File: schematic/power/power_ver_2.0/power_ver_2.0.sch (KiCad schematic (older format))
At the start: 47 parts, among them J1 PWM INPUT, J2 Audio OUTPUT, J3 Amp_Power, J4 Driver_power, Q1 IRF530A, Q2 IRF530A, Q3 IRF530A, Q4 IRF530A, U1 HIP4082IP

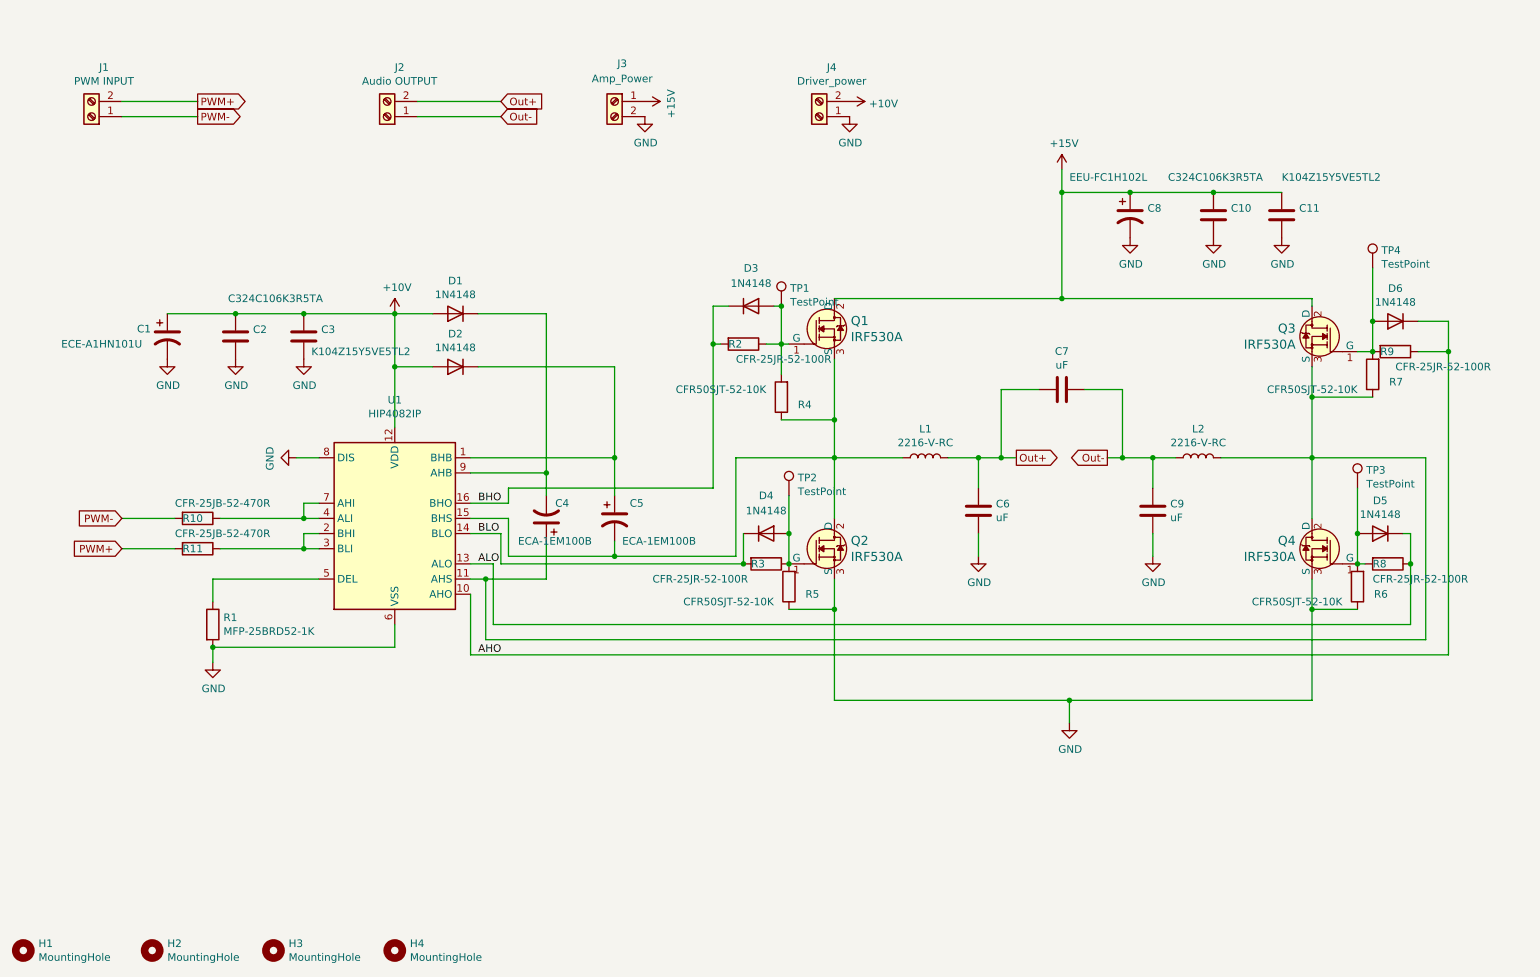
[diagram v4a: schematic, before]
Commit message: joint pcb power section
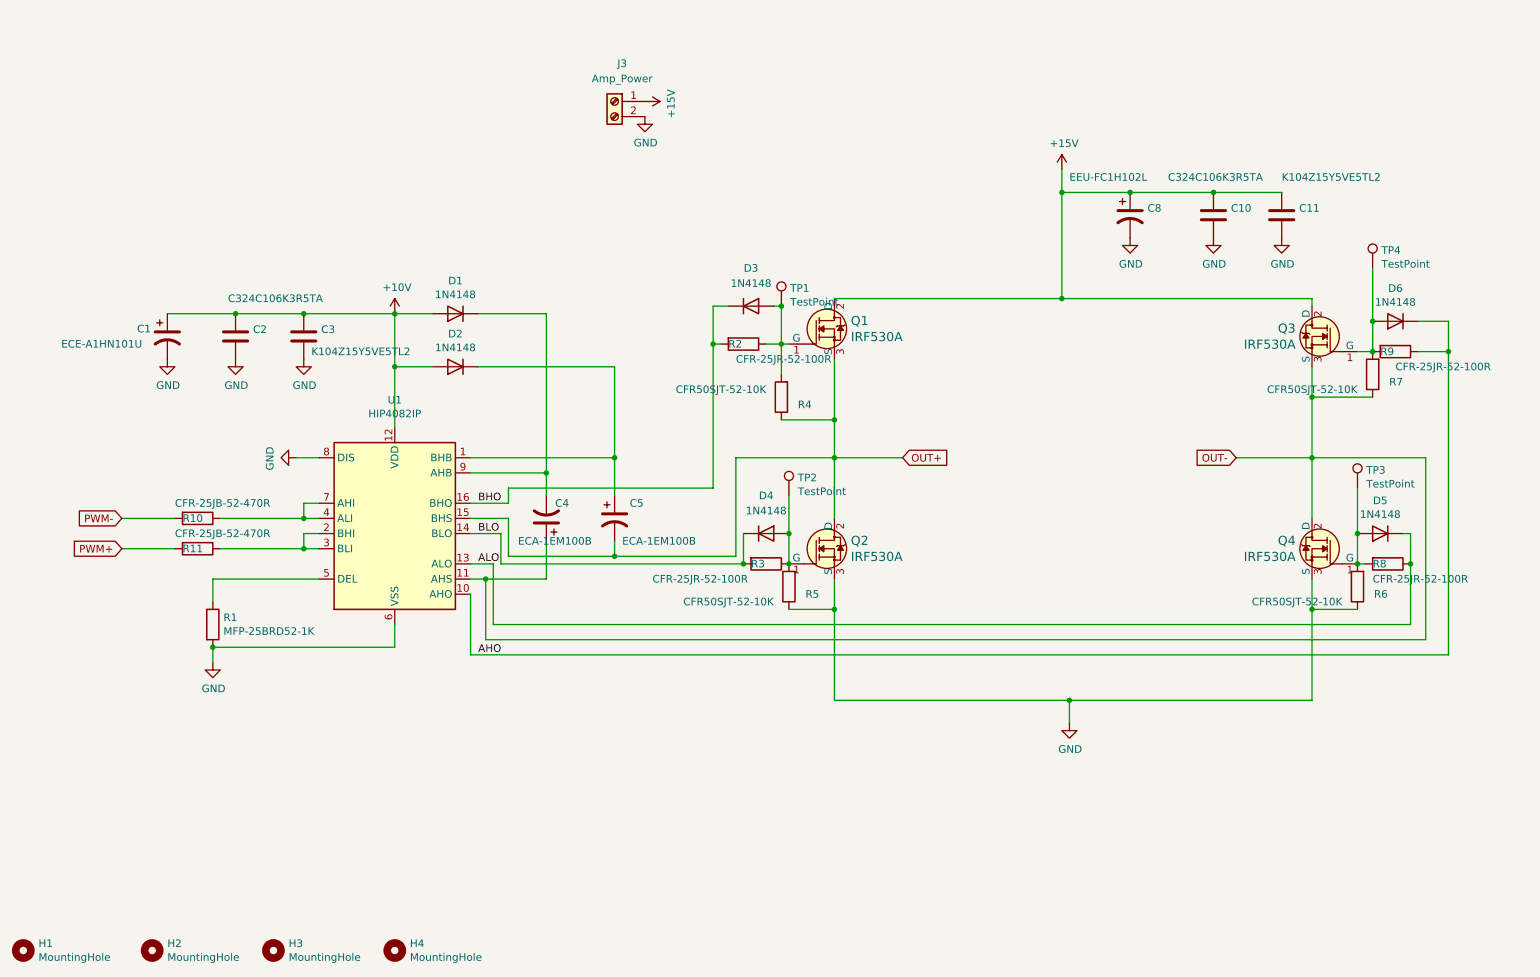
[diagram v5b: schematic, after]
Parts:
- removed C6, C7, C9: uF, Capacitor_THT:C_Radial_D10.0mm_H12.5mm_P5.00mm, symbol Device:C
- removed J1: PWM INPUT, TerminalBlock:TerminalBlock_Altech_AK300-2_P5.00mm, symbol Connector:Screw_Terminal_01x02
- removed J2: Audio OUTPUT, TerminalBlock:TerminalBlock_Altech_AK300-2_P5.00mm, symbol Connector:Screw_Terminal_01x02
- removed J4: Driver_power, TerminalBlock:TerminalBlock_Altech_AK300-2_P5.00mm, symbol Connector:Screw_Terminal_01x02
- removed L1, L2: 2216-V-RC, Inductor_THT:L_Toroid_Vertical_L24.6mm_W15.5mm_P11.44mm_Pulse_KM-4, symbol Device:L
- J3: footprint TerminalBlock:TerminalBlock_Altech_AK300-2_P5.00mm -> TerminalBlock_Phoenix:TerminalBlock_Phoenix_PT-1,5-2-3.5-H_1x02_P3.50mm_Horizontal
- U1: Digi-Key_PN (none) -> 2156-HIP4082IP-IL-ND
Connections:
- net OUT-: now reaches C4.1, Q3.3 (S), Q4.2 (D), R7.1, U1.11 (AHS)
- net OUT+: now reaches C5.2, Q1.3 (S), Q2.2 (D), R4.1, U1.15 (BHS)
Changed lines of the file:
@@
 F 3 "https://www.renesas.com/www/doc/datasheet/hip4082.pdf" H 3700 4900 50  0001 C CNN
 F 4 "Full bridge gate driver" H 3600 4150 50  0001 C CNN "Description"
+F 5 "2156-HIP4082IP-IL-ND" H 3600 4150 50  0001 C CNN "Digi-Key_PN"
 	1    3600 4150
 	1    0    0    -1
 $EndComp
-$Comp
-L Connector:Screw_Terminal_01x02 J1
-U 1 1 612E2854
-P 1600 1500
-F 0 "J1" H 1518 1175 50  0000 C CNN
-F 1 "PWM INPUT" H 1518 1266 50  0000 C CNN
-F 2 "TerminalBlock:TerminalBlock_Altech_AK300-2_P5.00mm" H 1600 1500 50  0001 C CNN
-F 3 "https://media.digikey.com/pdf/Data%20Sheets/Phoenix%20Contact%20PDFs/1935161.pdf" H 1600 1500 50  0001 C CNN
-F 4 "277-1667-ND" H 1600 1500 50  0001 C CNN "Digi-Key_PN"
-	1    1600 1500
-	-1   0    0    1
-$EndComp
-Text GLabel 2300 1400 2    50   Output ~ 0
-PWM+
-Wire Wire Line
-	1800 1400 2300 1400
-Text GLabel 2300 1500 2    50   Output ~ 0
-PWM-
-Wire Wire Line
-	1800 1500 2300 1500
 Text GLabel 1800 4350 0    50   Input ~ 0
 PWM+
@@
 Wire Wire Line
 	9650 3150 9650 3350
-$Comp
-L Device:L L1
-U 1 1 61319407
-P 7100 3750
-F 0 "L1" V 7290 3750 50  0000 C CNN
-F 1 "2216-V-RC" V 7199 3750 50  0000 C CNN
-F 2 "Inductor_THT:L_Toroid_Vertical_L24.6mm_W15.5mm_P11.44mm_Pulse_KM-4" H 7100 3750 50  0001 C CNN
-F 3 "~" H 7100 3750 50  0001 C CNN
-	1    7100 3750
-	0    -1   -1   0
-$EndComp
 Connection ~ 6500 3750
 Wire Wire Line
 	6500 3750 6500 4150
-Wire Wire Line
-	7600 3750 7600 3300
-Wire Wire Line
-	8400 3300 8400 3750
-Wire Wire Line
-	9050 3750 9650 3750
 Connection ~ 9650 3750
 Wire Wire Line
 	9650 3750 9650 4150
-$Comp
-L power:GND #PWR011
-U 1 1 6131F4E5
-P 7450 4400
-F 0 "#PWR011" H 7450 4150 50  0001 C CNN
-F 1 "GND" H 7455 4227 50  0000 C CNN
-F 2 "" H 7450 4400 50  0001 C CNN
-F 3 "" H 7450 4400 50  0001 C CNN
-	1    7450 4400
-	1    0    0    -1
-$EndComp
-Wire Wire Line
-	7450 4400 7450 4250
-$Comp
-L power:GND #PWR015
-U 1 1 6132039F
-P 8600 4400
-F 0 "#PWR015" H 8600 4150 50  0001 C CNN
-F 1 "GND" H 8605 4227 50  0000 C CNN
-F 2 "" H 8600 4400 50  0001 C CNN
-F 3 "" H 8600 4400 50  0001 C CNN
-	1    8600 4400
-	1    0    0    -1
-$EndComp
-Wire Wire Line
-	8600 4400 8600 4250
-Text GLabel 7700 3750 2    50   Output ~ 0
-Out+
-Text GLabel 8300 3750 0    50   Output ~ 0
-Out-
-$Comp
-L Connector:Screw_Terminal_01x02 J2
-U 1 1 613223B2
-P 3550 1500
-F 0 "J2" H 3468 1175 50  0000 C CNN
-F 1 "Audio OUTPUT" H 3468 1266 50  0000 C CNN
-F 2 "TerminalBlock:TerminalBlock_Altech_AK300-2_P5.00mm" H 3550 1500 50  0001 C CNN
-F 3 "https://media.digikey.com/pdf/Data%20Sheets/Phoenix%20Contact%20PDFs/1935161.pdf" H 3550 1500 50  0001 C CNN
-F 4 "277-1667-ND" H 3550 1500 50  0001 C CNN "Digi-Key_PN"
-	1    3550 1500
-	-1   0    0    1
-$EndComp
-Text GLabel 4300 1400 2    50   Input ~ 0
-Out+
-Text GLabel 4300 1500 2    50   Input ~ 0
-Out-
 Wire Wire Line
 	4350 4150 4350 4400
@@
 Wire Wire Line
 	9650 3750 10400 3750
-Wire Wire Line
-	8300 3750 8400 3750
-Connection ~ 8400 3750
-Wire Wire Line
-	7600 3750 7700 3750
-Connection ~ 7600 3750
 Connection ~ 3600 2800
 Wire Wire Line
@@
 $EndComp
 Wire Wire Line
-	7250 3750 7450 3750
-Wire Wire Line
-	7450 3950 7450 3750
-Connection ~ 7450 3750
-Wire Wire Line
-	7450 3750 7600 3750
-Wire Wire Line
-	8600 3950 8600 3750
-Wire Wire Line
-	8400 3750 8600 3750
-Connection ~ 8600 3750
-Wire Wire Line
-	8600 3750 8750 3750
-Wire Wire Line
-	7600 3300 7850 3300
-Wire Wire Line
-	8150 3300 8400 3300
-Wire Wire Line
 	8000 2000 8450 2000
 Connection ~ 8000 2000
@@
 F 0 "J3" H 5000 1650 50  0000 C CNN
 F 1 "Amp_Power" H 5000 1550 50  0000 C CNN
-F 2 "TerminalBlock:TerminalBlock_Altech_AK300-2_P5.00mm" H 5050 1400 50  0001 C CNN
+F 2 "TerminalBlock_Phoenix:TerminalBlock_Phoenix_PT-1,5-2-3.5-H_1x02_P3.50mm_Horizontal" H 5050 1400 50  0001 C CNN
 F 3 "https://media.digikey.com/pdf/Data%20Sheets/Phoenix%20Contact%20PDFs/1935161.pdf" H 5050 1400 50  0001 C CNN
 F 4 "277-1667-ND" H 5050 1400 50  0001 C CNN "Digi-Key_PN"
@@
 Wire Wire Line
 	3000 2800 3600 2800
-$Comp
-L Device:L L2
-U 1 1 614D4A87
-P 8900 3750
-F 0 "L2" V 9090 3750 50  0000 C CNN
-F 1 "2216-V-RC" V 8999 3750 50  0000 C CNN
-F 2 "Inductor_THT:L_Toroid_Vertical_L24.6mm_W15.5mm_P11.44mm_Pulse_KM-4" H 8900 3750 50  0001 C CNN
-F 3 "~" H 8900 3750 50  0001 C CNN
-	1    8900 3750
-	0    -1   -1   0
-$EndComp
-$Comp
-L Device:C C6
-U 1 1 614DAA49
-P 7450 4100
-F 0 "C6" H 7565 4146 50  0000 L CNN
-F 1 "uF" H 7565 4055 50  0000 L CNN
-F 2 "Capacitor_THT:C_Radial_D10.0mm_H12.5mm_P5.00mm" H 7488 3950 50  0001 C CNN
-F 3 "~" H 7450 4100 50  0001 C CNN
-F 4 "" H 7450 4100 50  0001 C CNN "Description"
-	1    7450 4100
-	1    0    0    -1
-$EndComp
-$Comp
-L Device:C C9
-U 1 1 614DB54C
-P 8600 4100
-F 0 "C9" H 8715 4146 50  0000 L CNN
-F 1 "uF" H 8715 4055 50  0000 L CNN
-F 2 "Capacitor_THT:C_Radial_D10.0mm_H12.5mm_P5.00mm" H 8638 3950 50  0001 C CNN
-F 3 "~" H 8600 4100 50  0001 C CNN
-F 4 "" H 8600 4100 50  0001 C CNN "Description"
-	1    8600 4100
-	1    0    0    -1
-$EndComp
-$Comp
-L Device:C C7
-U 1 1 614DC10B
-P 8000 3300
-F 0 "C7" V 7748 3300 50  0000 C CNN
-F 1 "uF" V 7839 3300 50  0000 C CNN
-F 2 "Capacitor_THT:C_Radial_D10.0mm_H12.5mm_P5.00mm" H 8038 3150 50  0001 C CNN
-F 3 "~" H 8000 3300 50  0001 C CNN
-F 4 "" H 8000 3300 50  0001 C CNN "Description"
-	1    8000 3300
-	0    1    1    0
-$EndComp
 Text GLabel 1800 4150 0    50   Input ~ 0
 PWM-
@@
 $EndComp
 $Comp
-L power:+10V #PWR09
-U 1 1 6136C310
-P 6600 1400
-F 0 "#PWR09" H 6600 1250 50  0001 C CNN
-F 1 "+10V" V 6615 1528 50  0000 L CNN
-F 2 "" H 6600 1400 50  0001 C CNN
-F 3 "" H 6600 1400 50  0001 C CNN
-	1    6600 1400
-	0    1    1    0
-$EndComp
-$Comp
 L power:+10V #PWR06
 U 1 1 6136ECB5
@@
 Text Label 4150 5050 0    50   ~ 0
 AHO
-Wire Wire Line
-	3750 1400 4300 1400
-Wire Wire Line
-	3750 1500 4300 1500
 $Comp
 L Connector:TestPoint TP2
@@
 	9950 4250 9950 4450
 $Comp
-L Connector:Screw_Terminal_01x02 J4
-U 1 1 614C15B1
-P 6400 1500
-F 0 "J4" H 6318 1175 50  0000 C CNN
-F 1 "Driver_power" H 6318 1266 50  0000 C CNN
-F 2 "TerminalBlock:TerminalBlock_Altech_AK300-2_P5.00mm" H 6400 1500 50  0001 C CNN
-F 3 "https://media.digikey.com/pdf/Data%20Sheets/Phoenix%20Contact%20PDFs/1935161.pdf" H 6400 1500 50  0001 C CNN
-F 4 "277-1667-ND" H 6400 1500 50  0001 C CNN "Digi-Key_PN"
-	1    6400 1500
-	-1   0    0    1
-$EndComp
-$Comp
 L Device:R R5
 U 1 1 613EB9C4
@@
 	1    0    0    -1
 $EndComp
-$Comp
-L power:GND #PWR010
-U 1 1 614CCA5B
-P 6600 1500
-F 0 "#PWR010" H 6600 1250 50  0001 C CNN
-F 1 "GND" H 6605 1327 50  0000 C CNN
-F 2 "" H 6600 1500 50  0001 C CNN
-F 3 "" H 6600 1500 50  0001 C CNN
-	1    6600 1500
-	1    0    0    -1
-$EndComp
 Wire Wire Line
 	6150 2750 6150 3000
@@
 	0    1    1    0
 $EndComp
+Text GLabel 6950 3750 2    50   Input ~ 0
+OUT+
+Text GLabel 9150 3750 0    50   Input ~ 0
+OUT-
+Wire Wire Line
+	9150 3750 9650 3750
 $EndSCHEMATC

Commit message: power 3.0 pcb layout
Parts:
- Q1, Q2, Q3, Q4: symbol dk_Transistors-FETs-MOSFETs-Single:IRF540NPBF -> power_ver_2.0-rescue:IRF540NPBF-dk_Transistors-FETs-MOSFETs-Single
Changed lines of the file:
@@
 	3000 4350 3100 4350
 $Comp
-L dk_Transistors-FETs-MOSFETs-Single:IRF540NPBF Q2
+L power_ver_2.0-rescue:IRF540NPBF-dk_Transistors-FETs-MOSFETs-Single Q2
 U 1 1 61356BCC
 P 6500 4350
@@
 	4350 3950 5700 3950
 $Comp
-L dk_Transistors-FETs-MOSFETs-Single:IRF540NPBF Q3
+L power_ver_2.0-rescue:IRF540NPBF-dk_Transistors-FETs-MOSFETs-Single Q3
 U 1 1 61314458
 P 9650 2950
@@
 $EndComp
 $Comp
-L dk_Transistors-FETs-MOSFETs-Single:IRF540NPBF Q4
+L power_ver_2.0-rescue:IRF540NPBF-dk_Transistors-FETs-MOSFETs-Single Q4
 U 1 1 6132015F
 P 9650 4350
@@
 $EndComp
 $Comp
-L dk_Transistors-FETs-MOSFETs-Single:IRF540NPBF Q1
+L power_ver_2.0-rescue:IRF540NPBF-dk_Transistors-FETs-MOSFETs-Single Q1
 U 1 1 613134AB
 P 6500 2900
